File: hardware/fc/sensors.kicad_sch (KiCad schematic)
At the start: 4 parts, among them U6 LSM6DSK320X

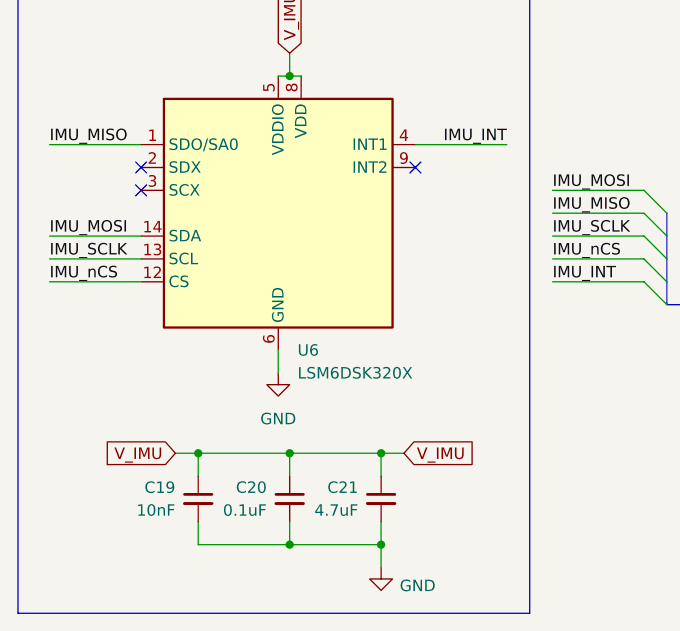
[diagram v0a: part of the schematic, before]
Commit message: fc: update schem to reflect ST datasheet
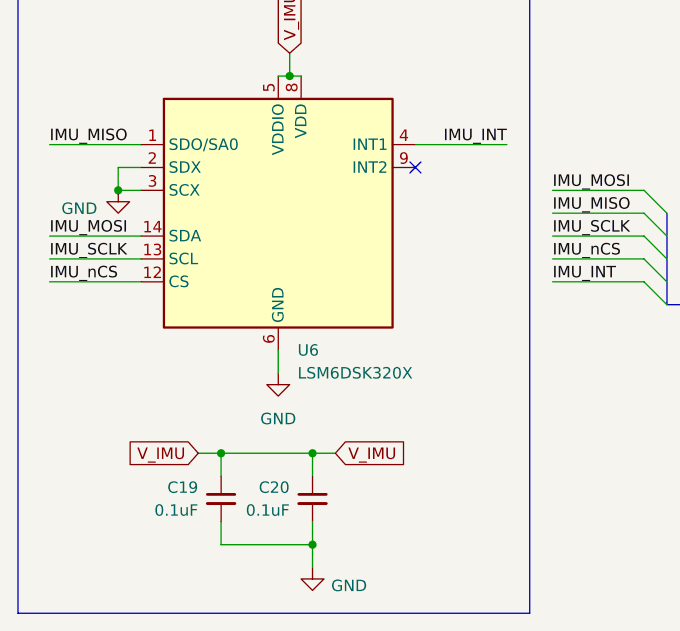
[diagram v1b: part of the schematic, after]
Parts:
- removed C21: 4.7uF, Stratus:C_0402, symbol Device:C_Small
- C19: value 10nF -> 0.1uF
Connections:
- net GND: now also U6.2 (SDX), U6.3 (SCX)
- no-connect marks 3 -> 1
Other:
- moved on the sheet: C19, C20

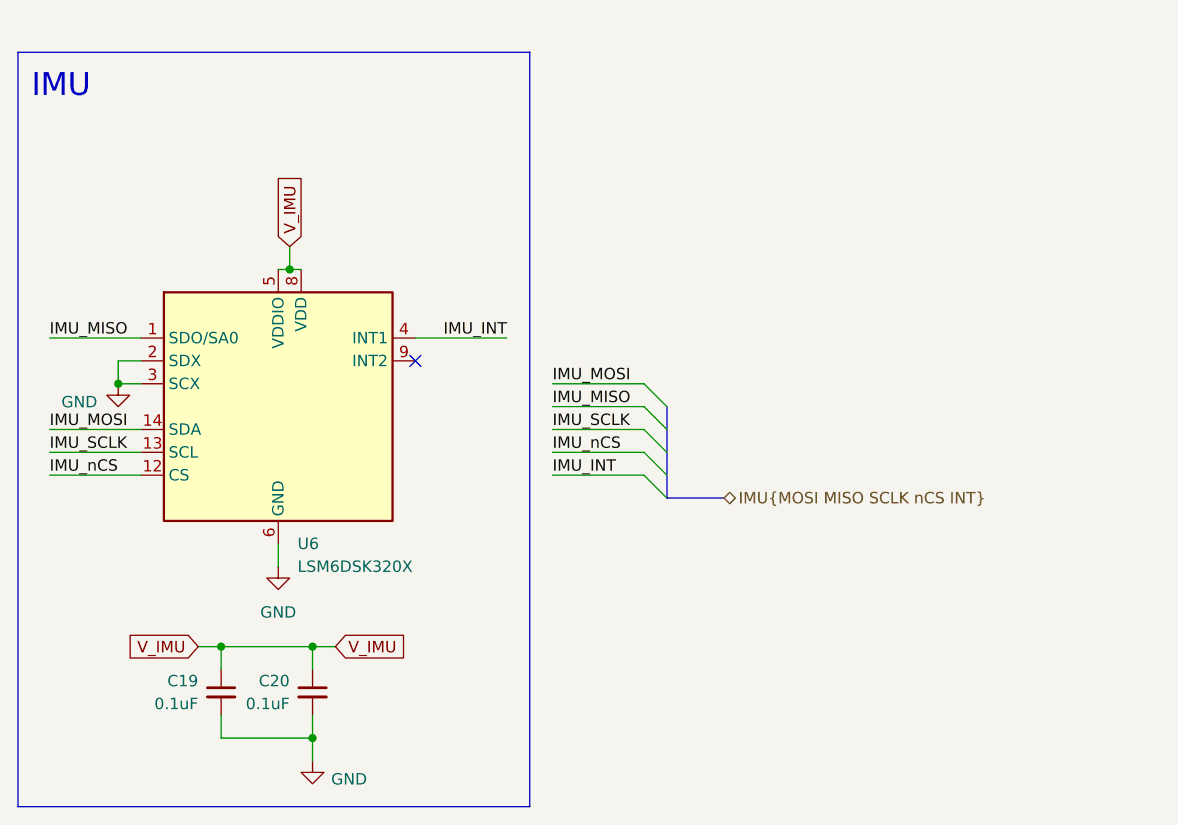
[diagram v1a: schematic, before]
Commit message: fc: schematic footprint changes
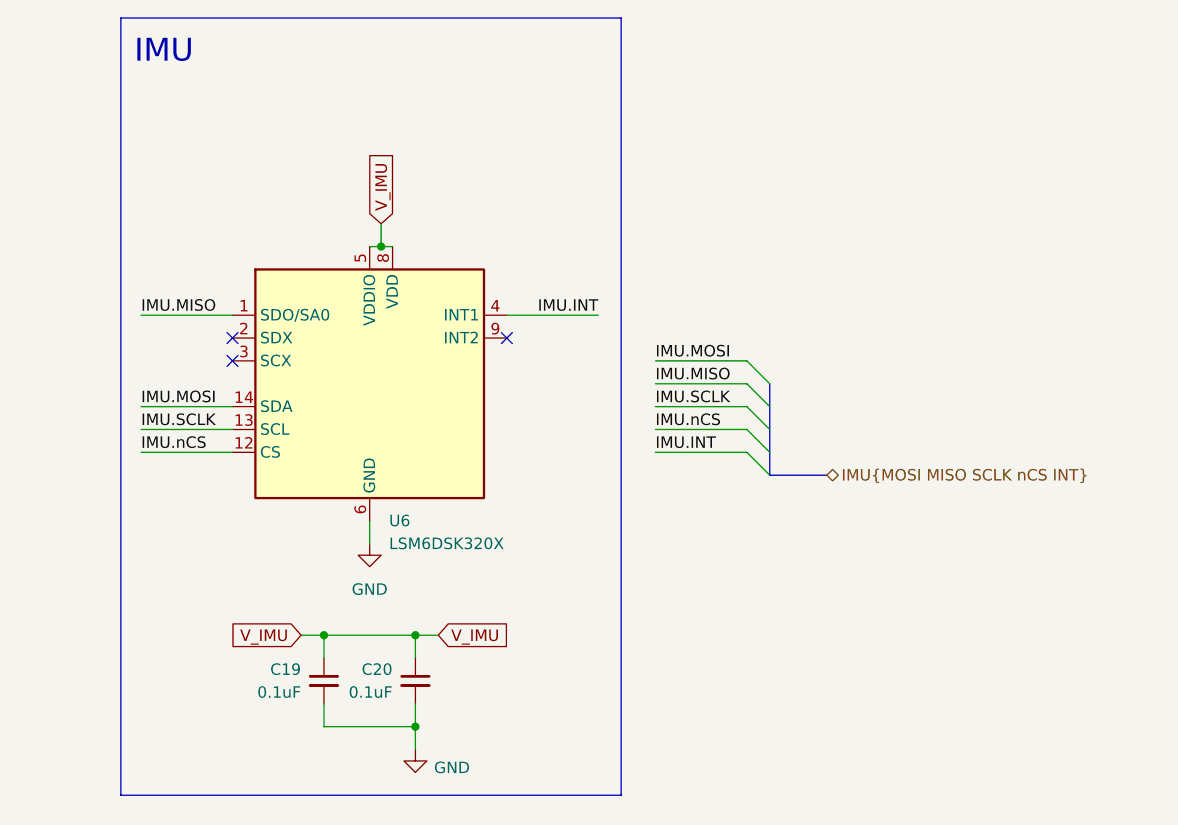
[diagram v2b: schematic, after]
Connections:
- net GND: no longer U6.2 (SDX), U6.3 (SCX)
- net IMU_INT renamed IMU.INT
- net IMU_MISO renamed IMU.MISO
- net IMU_MOSI renamed IMU.MOSI
- net IMU_SCLK renamed IMU.SCLK
- net IMU_nCS renamed IMU.nCS
- no-connect marks 1 -> 3
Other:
- moved on the sheet: C19, C20, U6

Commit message: fc: routing and pours
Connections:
- net GND: now also U6.2 (SDX), U6.3 (SCX)
- no-connect marks 3 -> 1
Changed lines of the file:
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@@
 	)
 	(rectangle
-		(start 109.5136 55.88)
+		(start 100.33 55.88)
 		(end 165.1 142.24)
 		(stroke
@@
 	(text "IMU"
 		(exclude_from_sim no)
-		(at 114.3 59.69 0)
+		(at 105.41 59.944 0)
 		(effects
 			(font
@@
 	)
 	(junction
+		(at 109.22 93.98)
+		(diameter 0)
+		(color 0 0 0 0)
+	)
+	(junction
 		(at 132.08 124.46)
 		(diameter 0)
@@
 	)
 	(no_connect
-		(at 121.92 93.98)
-	)
-	(no_connect
-		(at 121.92 91.44)
-	)
-	(no_connect
 		(at 152.4 91.44)
 	)
@@
 	(wire
 		(pts
+			(xy 109.22 96.52) (xy 109.22 93.98)
+		)
+		(stroke
+			(width 0)
+			(type default)
+		)
+	)
+	(wire
+		(pts
 			(xy 132.08 124.46) (xy 132.08 127)
 		)
@@
 	(wire
 		(pts
+			(xy 109.22 93.98) (xy 121.92 93.98)
+		)
+		(stroke
+			(width 0)
+			(type default)
+		)
+	)
+	(wire
+		(pts
 			(xy 152.4 88.9) (xy 162.56 88.9)
 		)
@@
 	(wire
 		(pts
+			(xy 121.92 91.44) (xy 109.22 91.44)
+		)
+		(stroke
+			(width 0)
+			(type default)
+		)
+	)
+	(wire
+		(pts
 			(xy 168.91 101.6) (xy 179.07 101.6)
 		)
@@
 		(pts
 			(xy 168.91 99.06) (xy 179.07 99.06)
+		)
+		(stroke
+			(width 0)
+			(type default)
+		)
+	)
+	(wire
+		(pts
+			(xy 109.22 91.44) (xy 109.22 93.98)
 		)
 		(stroke
@@
 					(unit 1)
 				)
+			)
+		)
+	)
+	(symbol
+		(lib_id "power:GND")
+		(at 109.22 96.52 0)
+		(unit 1)
+		(body_style 1)
+		(exclude_from_sim no)
+		(in_bom yes)
+		(on_board yes)
+		(in_pos_files yes)
+		(dnp no)
+		(property "Reference" "#PWR057"
+			(at 109.22 102.87 0)
+			(hide yes)
+			(show_name no)
+			(do_not_autoplace no)
+			(effects
+				(font
+					(size 1.27 1.27)
+				)
+			)
+		)
+		(property "Value" "GND"
+			(at 104.902 98.552 0)
+			(show_name no)
+			(do_not_autoplace no)
+			(effects
+				(font
+					(size 1.27 1.27)
+				)
+			)
+		)
+		(property "Footprint" ""
+			(at 109.22 96.52 0)
+			(hide yes)
+			(show_name no)
+			(do_not_autoplace no)
+			(effects
+				(font
+					(size 1.27 1.27)
+				)
+			)
+		)
+		(property "Datasheet" ""
+			(at 109.22 96.52 0)
+			(hide yes)
+			(show_name no)
+			(do_not_autoplace no)
+			(effects
+				(font
+					(size 1.27 1.27)
+				)
+			)
+		)
+		(property "Description" "Power symbol creates a global label with name \"GND\" , ground"
+			(at 109.22 96.52 0)
+			(hide yes)
+			(show_name no)
+			(do_not_autoplace no)
+			(effects
+				(font
+					(size 1.27 1.27)
+				)
+			)
+		)
+		(pin "1"
+		)
+		(instances
+			(project "fc"
+				(path "/6eb6d89e-9d71-4347-9ba3-a394c00e5720/a6d2d69b-2d48-4e76-8813-96121fd6287c"
+					(reference "#PWR057")
+					(unit 1)
+				)

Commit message: fc: footprints
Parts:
- U6: footprint Package_LGA:LGA-14_3x2.5mm_P0.5mm_LayoutBorder3x4y -> Stratus:LSM6DSK320X
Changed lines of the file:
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@@
 			)
 		)
-		(property "Footprint" "Package_LGA:LGA-14_3x2.5mm_P0.5mm_LayoutBorder3x4y"
+		(property "Footprint" "Stratus:LSM6DSK320X"
 			(at 127 114.3 0)
 			(hide yes)
